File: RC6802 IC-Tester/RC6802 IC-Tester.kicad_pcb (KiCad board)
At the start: 2 copper layers, 99.1 x 73 mm, 66 parts, among them J2 RC6802_UI_Port, M1 Mounting, M2 Mounting, M3 Mounting, M4 Mounting, Q1 2N3906, Q2 2N3906, Q3 2N3906, Q4 2N3904, Q5 2N3906, Q6 2N3904, SW1 RESET, SW2 PINS, SW3 ZIF_PWR, U1 74LS374, U2 74LS374, U3 ZIF-16

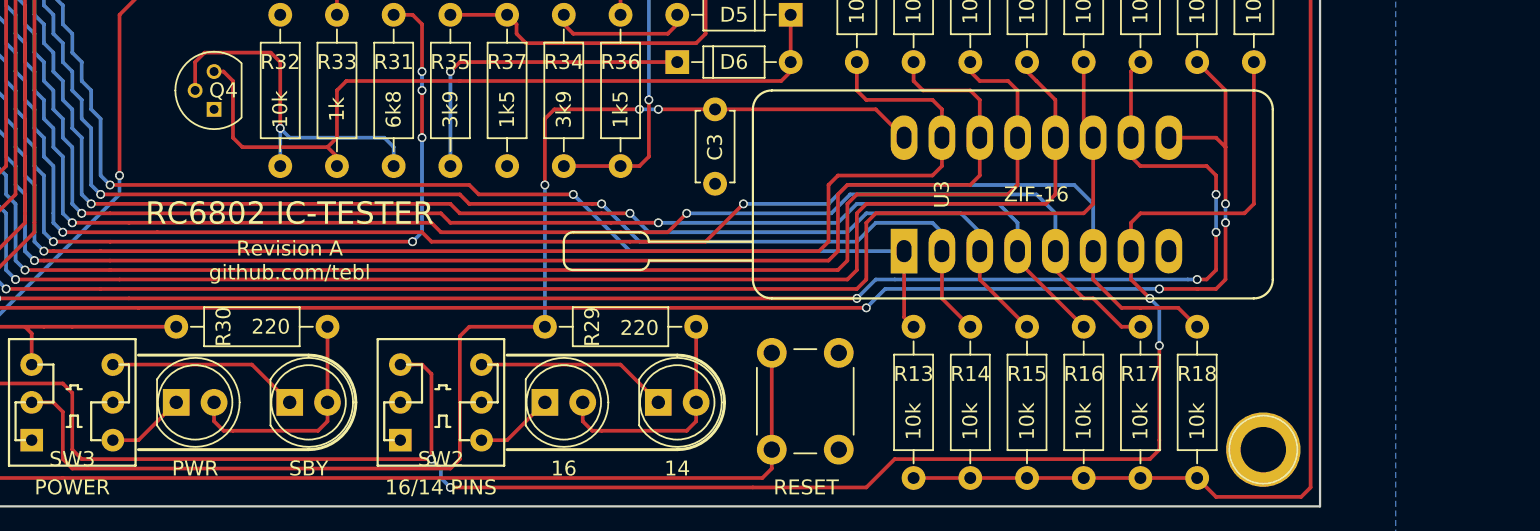
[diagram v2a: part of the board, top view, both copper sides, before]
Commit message: PWR/SBY LEDs swapped
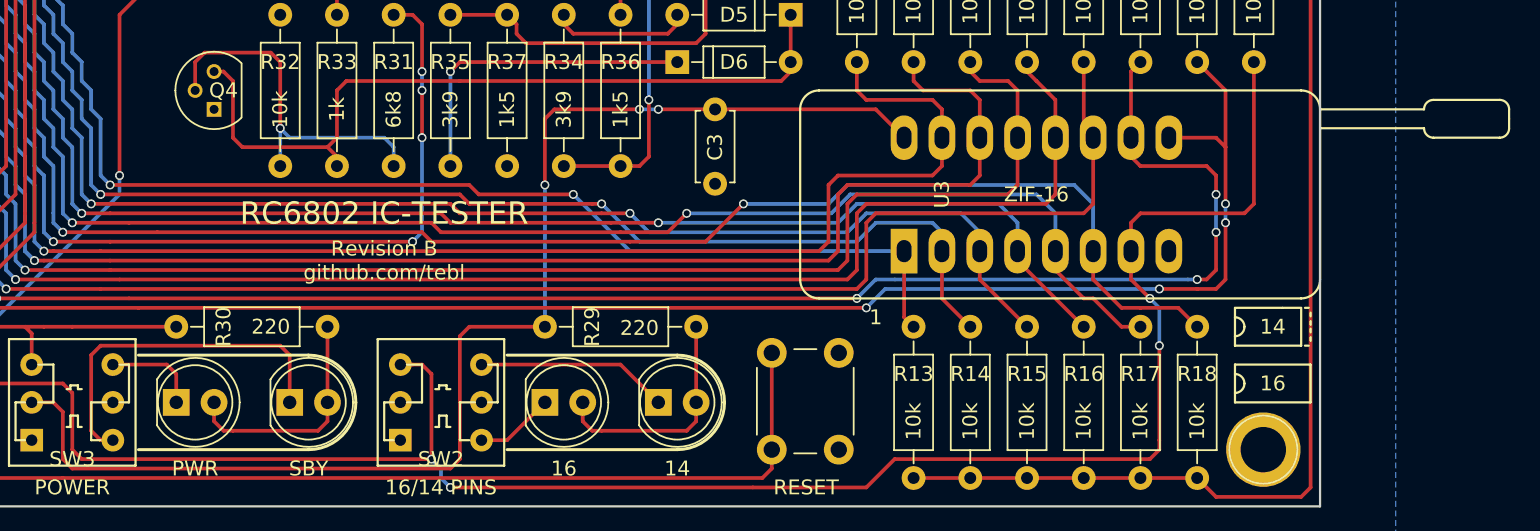
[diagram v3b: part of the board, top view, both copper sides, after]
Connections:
- SW3 pad 4: Net-(D4-Pad1) -> Net-(D3-Pad1)
- SW3 pad 6: Net-(D3-Pad1) -> Net-(D4-Pad1)
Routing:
- net Net-(D3-Pad1): track 12.9 -> 23.8 mm
- net Net-(D4-Pad1): track 5.31 -> 6.43 mm
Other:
- board text added: "1"
- board text added: "Revision B github.com/tebl"
- board text removed: "Revision A github.com/tebl"
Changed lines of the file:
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@@
     (area 100.254999 71.044999 199.465001 144.220001)
     (thickness 1.6)
-    (drawings 48)
-    (tracks 1068)
+    (drawings 51)
+    (tracks 1074)
     (zones 0)
     (modules 66)
@@
     (pad 1 thru_hole rect (at -2.725 2.54) (size 1.524 1.524) (drill 0.762) (layers *.Cu *.Mask))
     (pad 4 thru_hole circle (at 2.725 2.54) (size 1.524 1.524) (drill 0.762) (layers *.Cu *.Mask)
-      (net 14 "Net-(D4-Pad1)"))
+      (net 48 "Net-(D3-Pad1)"))
     (pad 5 thru_hole circle (at 2.725 0) (size 1.524 1.524) (drill 0.762) (layers *.Cu *.Mask)
       (net 1 GND))
     (pad 6 thru_hole circle (at 2.725 -2.54) (size 1.524 1.524) (drill 0.762) (layers *.Cu *.Mask)
-      (net 48 "Net-(D3-Pad1)"))
+      (net 14 "Net-(D4-Pad1)"))
   )
   (module Housings_DIP:DIP-20_W7.62mm_Socket (layer F.Cu)
@@
       (effects (font (size 1 1) (thickness 0.15)))
     )
-    (fp_line (start 10.795 23.495) (end 10.795 -8.89) (layer F.SilkS) (width 0.15))
-    (fp_line (start 0.635 -17.145) (end 0.635 -10.16) (layer F.SilkS) (width 0.15))
-    (fp_line (start -0.635 -17.145) (end -0.635 -10.16) (layer F.SilkS) (width 0.15))
-    (fp_line (start 1.27 -17.78) (end 1.27 -22.225) (layer F.SilkS) (width 0.15))
-    (fp_line (start -1.27 -22.225) (end -1.27 -17.78) (layer F.SilkS) (width 0.15))
-    (fp_arc (start -0.635 -17.78) (end -0.635 -17.145) (angle 90) (layer F.SilkS) (width 0.15))
-    (fp_arc (start 0.635 -17.78) (end 1.27 -17.78) (angle 90) (layer F.SilkS) (width 0.15))
-    (fp_arc (start 0.635 -22.225) (end 0.635 -22.86) (angle 90) (layer F.SilkS) (width 0.15))
-    (fp_arc (start -0.635 -22.225) (end -1.27 -22.225) (angle 90) (layer F.SilkS) (width 0.15))
-    (fp_line (start 0 -22.86) (end 0.635 -22.86) (layer F.SilkS) (width 0.15))
-    (fp_line (start -0.635 -22.86) (end 0 -22.86) (layer F.SilkS) (width 0.15))
-    (fp_line (start -3.175 -8.89) (end -3.175 23.495) (layer F.SilkS) (width 0.15))
-    (fp_line (start 9.525 -10.16) (end -1.905 -10.16) (layer F.SilkS) (width 0.15))
-    (fp_line (start -1.905 24.765) (end 9.525 24.765) (layer F.SilkS) (width 0.15))
-    (fp_arc (start -1.905 -8.89) (end -3.175 -8.89) (angle 90) (layer F.SilkS) (width 0.15))
-    (fp_arc (start 9.525 -8.89) (end 9.525 -10.16) (angle 90) (layer F.SilkS) (width 0.15))
-    (fp_arc (start 9.525 23.495) (end 10.795 23.495) (angle 90) (layer F.SilkS) (width 0.15))
-    (fp_arc (start -1.905 23.495) (end -1.905 24.765) (angle 90) (layer F.SilkS) (width 0.15))
+    (fp_line (start -6.0325 27.305) (end -5.7785 27.305) (layer F.SilkS) (width 0.15))
+    (fp_line (start -5.207 27.305) (end -5.461 27.305) (layer F.SilkS) (width 0.15))
+    (fp_line (start -4.699 27.305) (end -4.953 27.305) (layer F.SilkS) (width 0.15))
+    (fp_line (start -4.1275 27.305) (end -4.3815 27.305) (layer F.SilkS) (width 0.15))
+    (fp_line (start -3.81 26.924) (end -3.81 27.178) (layer F.SilkS) (width 0.15))
+    (fp_line (start -6.35 27.178) (end -6.35 26.924) (layer F.SilkS) (width 0.15))
+    (fp_text user 14 (at -5.08 24.765 180) (layer F.SilkS)
+      (effects (font (size 1 1) (thickness 0.15)))
+    )
+    (fp_text user 16 (at -8.89 24.765 360) (layer F.SilkS)
+      (effects (font (size 1 1) (thickness 0.15)))
+    )
+    (fp_line (start -10.16 22.225) (end -7.62 22.225) (layer F.SilkS) (width 0.15))
+    (fp_line (start -7.62 22.225) (end -7.62 27.305) (layer F.SilkS) (width 0.15))
+    (fp_line (start -7.62 27.305) (end -10.16 27.305) (layer F.SilkS) (width 0.15))
+    (fp_line (start -10.16 27.305) (end -10.16 22.225) (layer F.SilkS) (width 0.15))
+    (fp_arc (start -8.89 22.225) (end -8.255 22.225) (angle 90) (layer F.SilkS) (width 0.15))
+    (fp_arc (start -8.89 22.225) (end -8.89 22.86) (angle 90) (layer F.SilkS) (width 0.15))
+    (fp_line (start -6.35 22.225) (end -6.35 26.67) (layer F.SilkS) (width 0.15))
+    (fp_line (start -6.35 26.67) (end -3.81 26.67) (layer F.SilkS) (width 0.15))
+    (fp_line (start -3.81 26.67) (end -3.81 25.4) (layer F.SilkS) (width 0.15))
+    (fp_line (start -6.35 22.225) (end -3.81 22.225) (layer F.SilkS) (width 0.15))
+    (fp_line (start -3.81 22.225) (end -3.81 25.4) (layer F.SilkS) (width 0.15))
+    (fp_arc (start -5.08 22.225) (end -5.08 22.86) (angle 90) (layer F.SilkS) (width 0.15))
+    (fp_arc (start -5.08 22.225) (end -4.445 22.225) (angle 90) (layer F.SilkS) (width 0.15))
+    (fp_line (start 10.795 26.67) (end 10.795 -5.715) (layer F.SilkS) (width 0.15))
+    (fp_line (start 9.525 27.94) (end 9.525 34.925) (layer F.SilkS) (width 0.15))
+    (fp_line (start 8.255 27.94) (end 8.255 34.925) (layer F.SilkS) (width 0.15))
+    (fp_line (start 7.62 35.56) (end 7.62 40.005) (layer F.SilkS) (width 0.15))
+    (fp_line (start 10.16 40.005) (end 10.16 35.56) (layer F.SilkS) (width 0.15))
+    (fp_arc (start 9.525 35.56) (end 9.525 34.925) (angle 90) (layer F.SilkS) (width 0.15))
+    (fp_arc (start 8.255 35.56) (end 7.62 35.56) (angle 90) (layer F.SilkS) (width 0.15))
+    (fp_arc (start 8.255 40.005) (end 8.255 40.64) (angle 90) (layer F.SilkS) (width 0.15))
+    (fp_arc (start 9.525 40.005) (end 10.16 40.005) (angle 90) (layer F.SilkS) (width 0.15))
+    (fp_line (start 8.89 40.64) (end 8.255 40.64) (layer F.SilkS) (width 0.15))
+    (fp_line (start 9.525 40.64) (end 8.89 40.64) (layer F.SilkS) (width 0.15))
+    (fp_line (start -3.175 -5.715) (end -3.175 26.67) (layer F.SilkS) (width 0.15))
+    (fp_line (start 9.525 -6.985) (end -1.905 -6.985) (layer F.SilkS) (width 0.15))
+    (fp_line (start -1.905 27.94) (end 9.525 27.94) (layer F.SilkS) (width 0.15))
+    (fp_arc (start -1.905 -5.715) (end -3.175 -5.715) (angle 90) (layer F.SilkS) (width 0.15))
+    (fp_arc (start 9.525 -5.715) (end 9.525 -6.985) (angle 90) (layer F.SilkS) (width 0.15))
+    (fp_arc (start 9.525 26.67) (end 10.795 26.67) (angle 90) (layer F.SilkS) (width 0.15))
+    (fp_arc (start -1.905 26.67) (end -1.905 27.94) (angle 90) (layer F.SilkS) (width 0.15))
     (fp_text user %R (at 3.81 2.54 90) (layer F.Fab)
       (effects (font (size 1 1) (thickness 0.15)))
@@
     )
   )
+  (gr_arc (start 169.545 123.19) (end 170.18 123.19) (angle 90) (layer B.SilkS) (width 0.2))
+  (gr_arc (start 169.545 123.19) (end 169.545 122.555) (angle 90) (layer B.SilkS) (width 0.2))
+  (gr_text 1 (at 169.545 131.445) (layer F.SilkS)
+    (effects (font (size 1 1) (thickness 0.15)))
+  )
   (gr_text "16 OR 14 PIN\nIC TO BE TESTED" (at 180.34 123.19) (layer B.SilkS)
     (effects (font (size 1 1) (thickness 0.15)) (justify mirror))
@@
   (gr_line (start 169.545 119.38) (end 169.545 127) (angle 90) (layer B.SilkS) (width 0.2))
   (gr_line (start 170.815 119.38) (end 169.545 119.38) (angle 90) (layer B.SilkS) (width 0.2))
-  (gr_text "Revision A\ngithub.com/tebl" (at 130.175 127.635) (layer F.SilkS)
+  (gr_text "Revision B\ngithub.com/tebl" (at 136.525 127.635) (layer F.SilkS)
     (effects (font (size 1 1) (thickness 0.15)))
   )
@@
     (effects (font (size 0.8 0.8) (thickness 0.1)) (justify mirror))
   )
-  (gr_text "RC6802 IC-TESTER" (at 130.175 124.46) (layer F.SilkS)
+  (gr_text "RC6802 IC-TESTER" (at 136.525 124.46) (layer F.SilkS)
     (effects (font (size 1.5 1.5) (thickness 0.3)))
   )
@@
   (segment (start 149.86 138.43) (end 149.86 137.16) (width 0.25) (layer F.Cu) (net 13))
   (segment (start 150.495 139.065) (end 149.86 138.43) (width 0.25) (layer F.Cu) (net 13))
-  (segment (start 118.295 139.7) (end 120.015 139.7) (width 0.25) (layer F.Cu) (net 14))
-  (segment (start 120.015 139.7) (end 122.555 137.16) (width 0.25) (layer F.Cu) (net 14))
+  (segment (start 118.295 134.62) (end 121.92 134.62) (width 0.25) (layer F.Cu) (net 14))
+  (segment (start 122.555 135.255) (end 122.555 137.16) (width 0.25) (layer F.Cu) (net 14))
+  (segment (start 121.92 134.62) (end 122.555 135.255) (width 0.25) (layer F.Cu) (net 14))
   (segment (start 114.935 142.24) (end 107.315 142.24) (width 0.25) (layer F.Cu) (net 15))
   (segment (start 162.56 141.605) (end 161.925 142.24) (width 0.25) (layer F.Cu) (net 15))
@@
   (segment (start 143.06 139.7) (end 144.78 139.7) (width 0.25) (layer F.Cu) (net 47))
   (segment (start 144.78 139.7) (end 147.32 137.16) (width 0.25) (layer F.Cu) (net 47))
-  (segment (start 118.295 134.62) (end 127.635 134.62) (width 0.25) (layer F.Cu) (net 48))
-  (segment (start 127.635 134.62) (end 130.175 137.16) (width 0.25) (layer F.Cu) (net 48))
+  (segment (start 118.295 139.7) (end 117.475 139.7) (width 0.25) (layer F.Cu) (net 48))
+  (segment (start 130.175 133.985) (end 130.175 137.16) (width 0.25) (layer F.Cu) (net 48))
+  (segment (start 129.54 133.35) (end 130.175 133.985) (width 0.25) (layer F.Cu) (net 48))
+  (segment (start 117.475 133.35) (end 129.54 133.35) (width 0.25) (layer F.Cu) (net 48))
+  (segment (start 116.84 133.985) (end 117.475 133.35) (width 0.25) (layer F.Cu) (net 48))
+  (segment (start 116.84 139.065) (end 116.84 133.985) (width 0.25) (layer F.Cu) (net 48))
+  (segment (start 117.475 139.7) (end 116.84 139.065) (width 0.25) (layer F.Cu) (net 48))
   (segment (start 132.715 137.16) (end 132.715 132.08) (width 0.25) (layer F.Cu) (net 49))
   (segment (start 126.365 139.065) (end 125.73 139.065) (width 0.25) (layer F.Cu) (net 49))
